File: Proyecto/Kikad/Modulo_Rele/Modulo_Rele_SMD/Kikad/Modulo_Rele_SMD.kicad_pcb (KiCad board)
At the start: 2 copper layers, 48.9 x 19 mm, 11 parts, among them J1 TB_1X3, J2 TB_1X3, K1 RELAY_C, Q1 BC337, U3 PC817

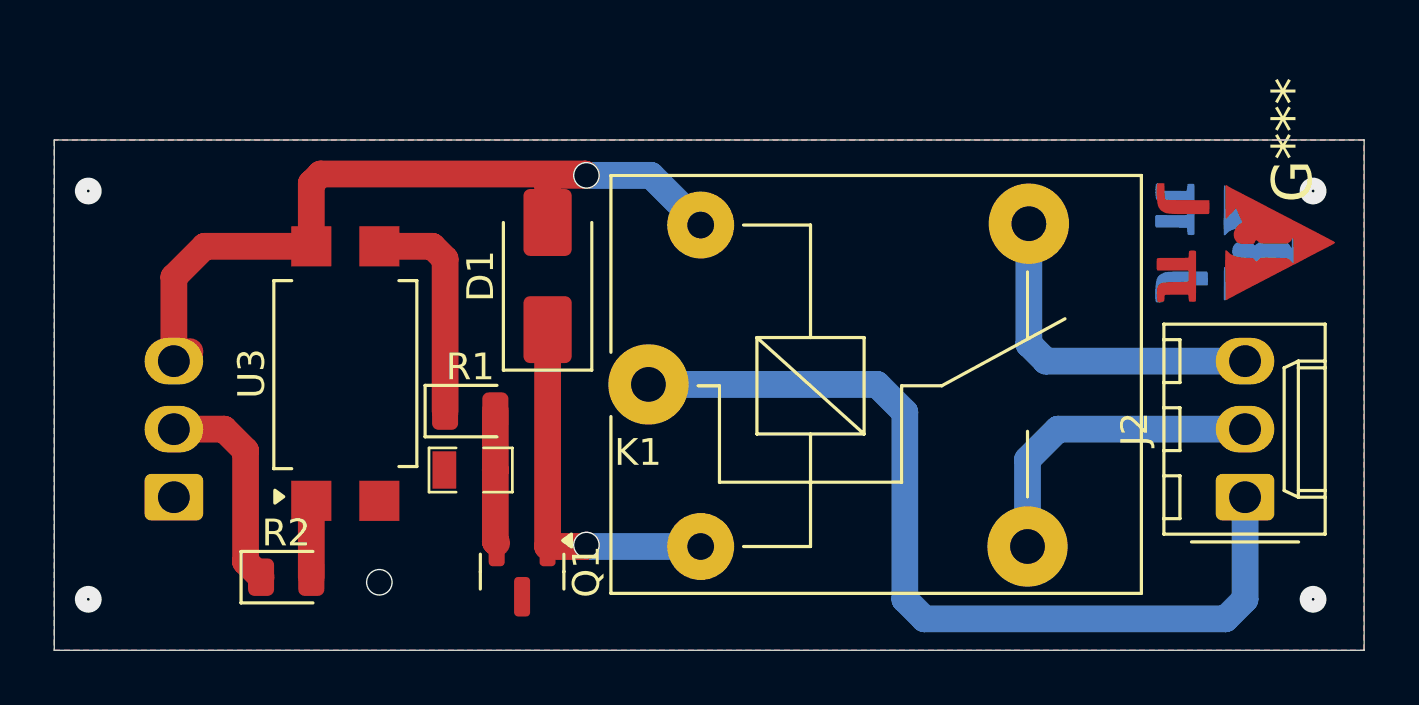
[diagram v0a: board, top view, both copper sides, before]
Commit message: Agregue la carpeta Placa_Principal e hice unas correcciones en el Modulo_Rele
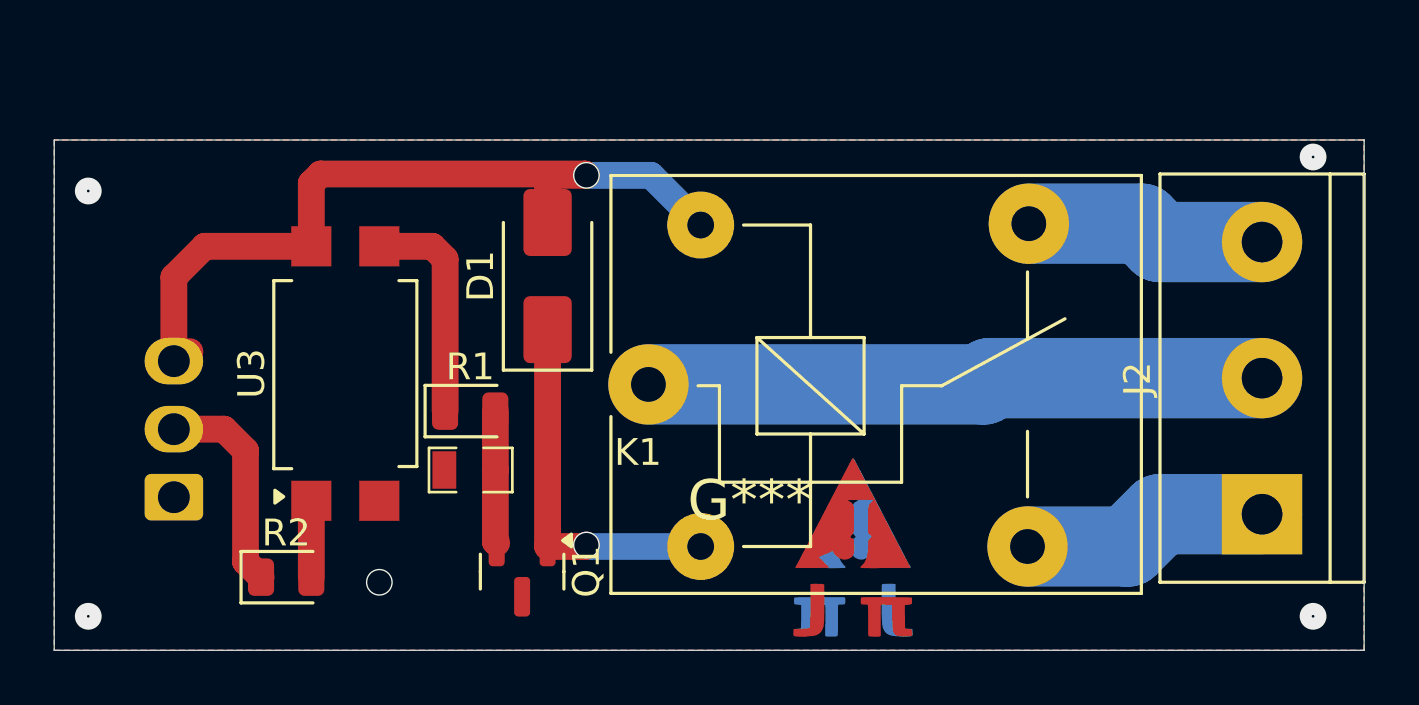
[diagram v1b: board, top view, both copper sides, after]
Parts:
- J2: footprint Connector_Molex:Molex_KK-254_AE-6410-03A_1x03_P2.54mm_Vertical -> TerminalBlock:TerminalBlock_bornier-3_P5.08mm
- moved G*** 18.6 mm to (144.7, 121.9), turned to 0 degrees
- moved G*** 18.5 mm to (144.8, 121.9), turned to 180 degrees
- moved J2 0.90 mm to (160.0, 120.7)
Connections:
- K1 pad 1: Net-(J2-Pad1) -> Net-(J2-Pad2)
- K1 pad 3: Net-(J2-Pad2) -> Net-(J2-Pad1)
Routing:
- net Net-(J2-Pad1): track 34.1 -> 9.25 mm
- net Net-(J2-Pad2): track 11.8 -> 23.0 mm
- net Net-(J2-Pad3): track 12.8 -> 8.99 mm
